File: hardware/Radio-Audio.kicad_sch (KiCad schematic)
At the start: 9 parts, among them J1 Conn_01x02_MountingPin, U1 LM386

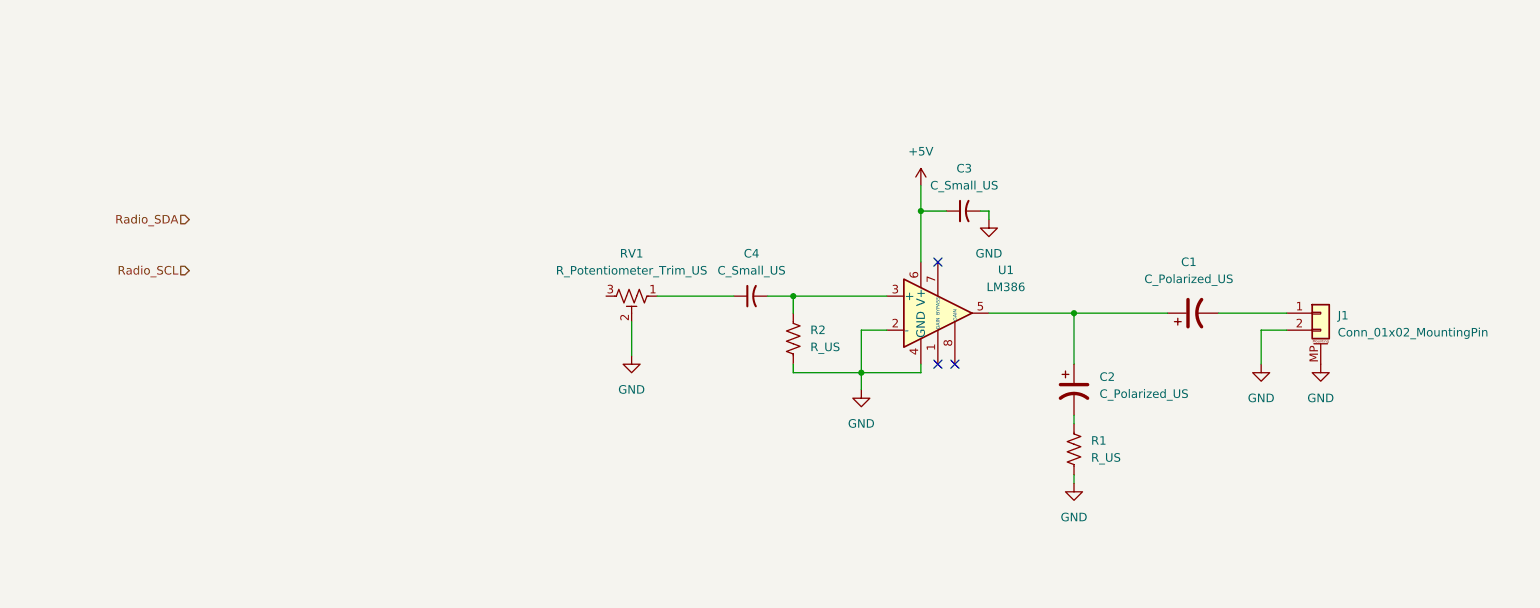
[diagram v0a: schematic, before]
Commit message: Added Radio Module to circuit
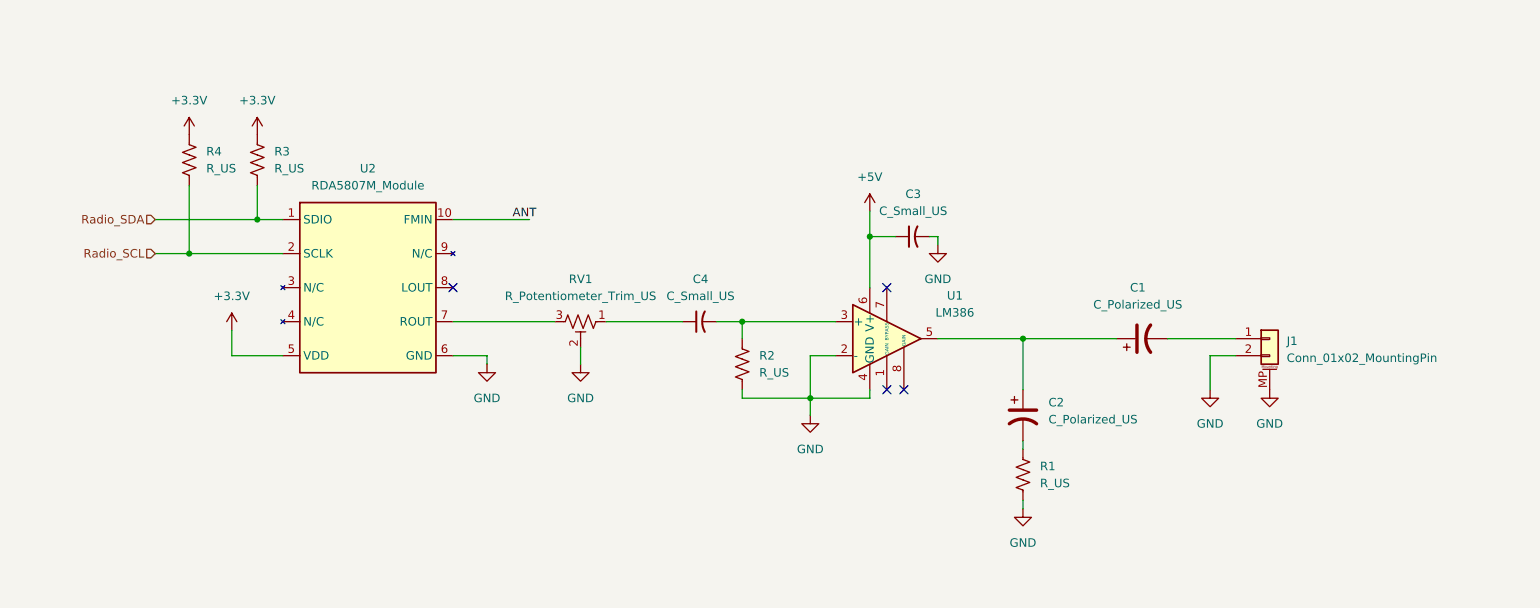
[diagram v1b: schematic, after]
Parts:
- added R3, R4: R_US, symbol Device:R_US
- added U2: RDA5807M_Module, ECE:RDA5807M_Module_TH, symbol ECE:RDA5807M_Module
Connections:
- net GND: now also U2.6 (GND)
- net Radio_SCL: now also R4.2, U2.2 (SCLK)
- net Radio_SDA: now also R3.1, U2.1 (SDIO)
- net at RV1.3: now also U2.7 (ROUT)
- new net +3.3V: R3.2, R4.1, U2.5 (VDD)
- new net ANT: U2.10 (FMIN)
- no-connect marks 3 -> 4
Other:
- moved on the sheet: C1, C2, C3, C4, J1, R1, R2, RV1, U1

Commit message: Assigned Pinout to Subsystems
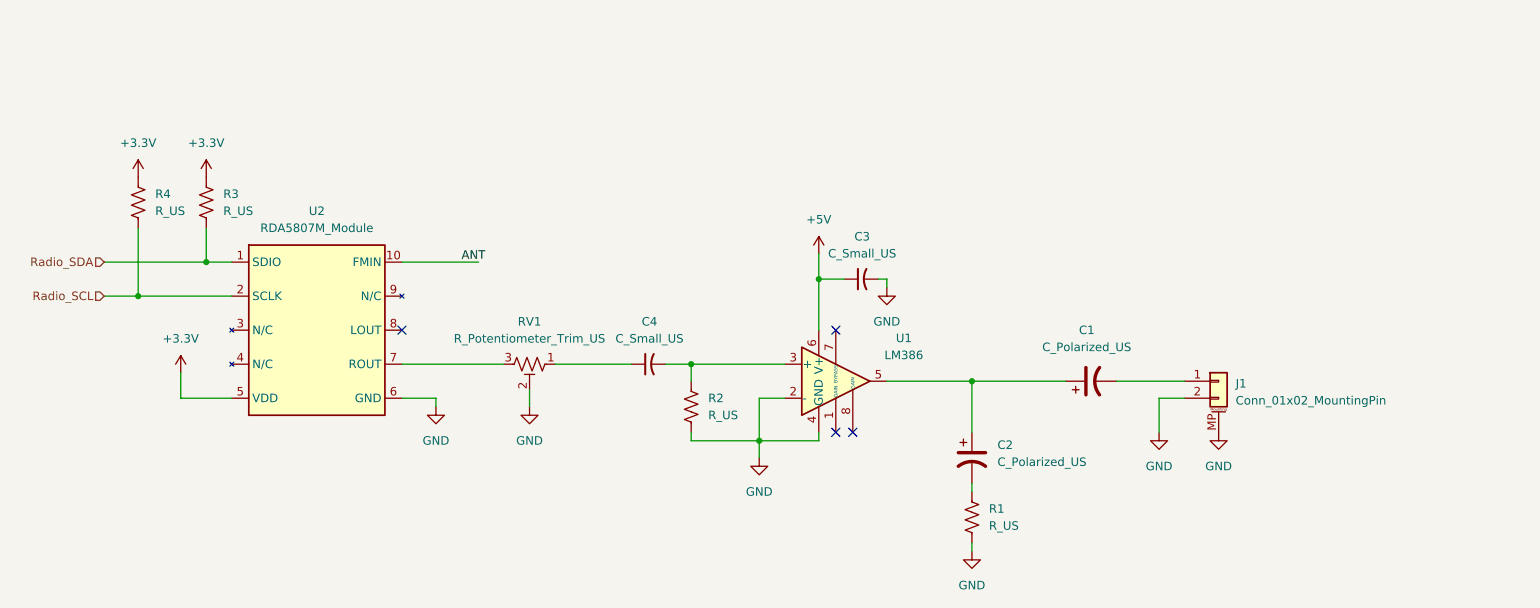
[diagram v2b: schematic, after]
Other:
- moved on the sheet: C1, C2, C3, C4, J1, R1, R2, R3, R4, RV1, U1, U2

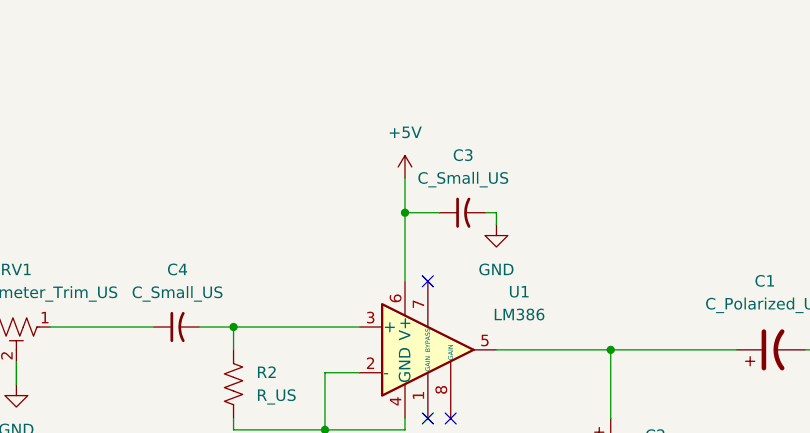
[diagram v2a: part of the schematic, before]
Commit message: Powerchain
Powerchain first draft done
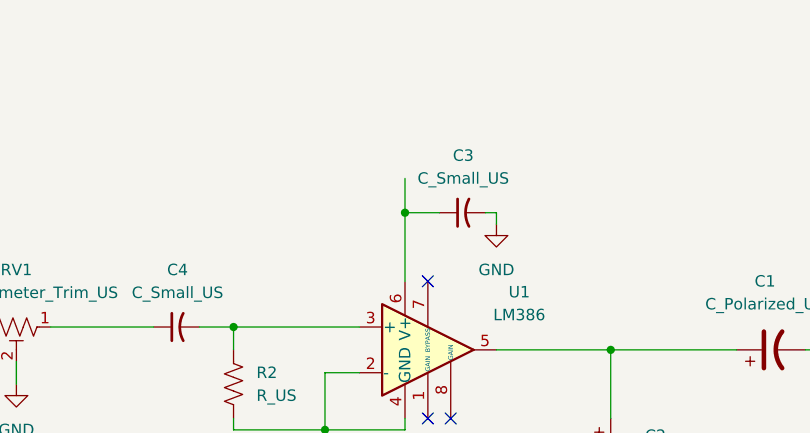
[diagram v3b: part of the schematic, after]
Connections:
- net +5V: no longer names the net of C3.1, U1.6 (V+)
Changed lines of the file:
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@@
-	)
-	(symbol
-		(lib_id "power:+5V")
-		(at 167.64 86.36 0)
-		(unit 1)
-		(exclude_from_sim no)
-		(in_bom yes)
-		(on_board yes)
-		(dnp no)
-		(fields_autoplaced yes)
-		(property "Reference" "#PWR07"
-			(at 167.64 90.17 0)
-			(effects
-				(font
-					(size 1.27 1.27)
-				)
-				(hide yes)
-			)
-		)
-		(property "Value" "+5V"
-			(at 167.64 81.28 0)
-			(effects
-				(font
-					(size 1.27 1.27)
-				)
-			)
-		)
-		(property "Footprint" ""
-			(at 167.64 86.36 0)
-			(effects
-				(font
-					(size 1.27 1.27)
-				)
-				(hide yes)
-			)
-		)
-		(property "Datasheet" ""
-			(at 167.64 86.36 0)
-			(effects
-				(font
-					(size 1.27 1.27)
-				)
-				(hide yes)
-			)
-		)
-		(property "Description" "Power symbol creates a global label with name \"+5V\""
-			(at 167.64 86.36 0)
-			(effects
-				(font
-					(size 1.27 1.27)
-				)
-				(hide yes)
-			)
-		)
-		(pin "1"
-		)
-		(instances
-			(project ""
-				(path "/adf646d2-aa7c-4345-9423-7107505b3b06/1b91a94e-3823-4ebf-b09f-64912f681b22"
-					(reference "#PWR07")
-					(unit 1)
-				)
-			)
-		)
 	)
 	(symbol

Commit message: Added Button circuit
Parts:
- added AE1: Antenna, symbol Device:Antenna
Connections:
- net +5V: now reaches C3.1, U1.6 (V+)
- net ANT: no longer names the net of U2.10 (FMIN)
- net ANT: now also AE1.1 (A)
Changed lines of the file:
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@@
-	(wire
-		(pts
-			(xy 105.41 87.63) (xy 116.84 87.63)
-		)
-		(stroke
-			(width 0)
-			(type default)
-		)
-	)
 	(wire
 		(pts
@@
 	(wire
 		(pts
+			(xy 105.41 87.63) (xy 113.03 87.63)
+		)
+		(stroke
+			(width 0)
+			(type default)
+		)
+	)
+	(wire
+		(pts
 			(xy 190.5 105.41) (xy 190.5 113.03)
 		)
@@
 	(wire
 		(pts
+			(xy 113.03 87.63) (xy 113.03 80.01)
+		)
+		(stroke
+			(width 0)
+			(type default)
+		)
+	)
+	(wire
+		(pts
 			(xy 148.59 114.3) (xy 158.75 114.3)
 		)
@@
 			(width 0)
 			(type default)
-		)
-	)
-	(label "ANT"
-		(at 114.3 87.63 0)
-		(effects
-			(font
-				(size 1.27 1.27)
-			)
-			(justify left bottom)
 		)
 	)
@@
 	)
 	(symbol
+		(lib_id "Device:Antenna")
+		(at 113.03 74.93 0)
+		(unit 1)
+		(exclude_from_sim no)
+		(in_bom yes)
+		(on_board yes)
+		(dnp no)
+		(fields_autoplaced yes)
+		(property "Reference" "AE1"
+			(at 115.57 74.2949 0)
+			(effects
+				(font
+					(size 1.27 1.27)
+				)
+				(justify left)
+			)
+		)
+		(property "Value" "Antenna"
+			(at 115.57 76.8349 0)
+			(effects
+				(font
+					(size 1.27 1.27)
+				)
+				(justify left)
+			)
+		)
+		(property "Footprint" ""
+			(at 113.03 74.93 0)
+			(effects
+				(font
+					(size 1.27 1.27)
+				)
+				(hide yes)
+			)
+		)
+		(property "Datasheet" "~"
+			(at 113.03 74.93 0)
+			(effects
+				(font
+					(size 1.27 1.27)
+				)
+				(hide yes)
+			)
+		)
+		(property "Description" "Antenna"
+			(at 113.03 74.93 0)
+			(effects
+				(font
+					(size 1.27 1.27)
+				)
+				(hide yes)
+			)
+		)
+		(pin "1"
+		)
+		(instances
+			(project ""
+				(path "/adf646d2-aa7c-4345-9423-7107505b3b06/1b91a94e-3823-4ebf-b09f-64912f681b22"
+					(reference "AE1")
+					(unit 1)
+				)
+			)
+		)
+	)
+	(symbol
 		(lib_id "Device:R_US")
 		(at 148.59 109.22 0)
@@
 					(unit 1)
 				)
+			)
+		)
+	)
+	(symbol
+		(lib_id "power:+5V")
+		(at 167.64 86.36 0)
+		(unit 1)
+		(exclude_from_sim no)
+		(in_bom yes)
+		(on_board yes)
+		(dnp no)
+		(fields_autoplaced yes)
+		(property "Reference" "#PWR028"
+			(at 167.64 90.17 0)
+			(effects
+				(font
+					(size 1.27 1.27)
+				)
+				(hide yes)
+			)
+		)
+		(property "Value" "+5V"
+			(at 167.64 81.28 0)
+			(effects
+				(font
+					(size 1.27 1.27)
+				)
+			)
+		)
+		(property "Footprint" ""
+			(at 167.64 86.36 0)
+			(effects
+				(font
+					(size 1.27 1.27)
+				)
+				(hide yes)
+			)
+		)
+		(property "Datasheet" ""
+			(at 167.64 86.36 0)
+			(effects
+				(font
+					(size 1.27 1.27)
+				)
+				(hide yes)
+			)
+		)
+		(property "Description" "Power symbol creates a global label with name \"+5V\""
+			(at 167.64 86.36 0)
+			(effects
+				(font
+					(size 1.27 1.27)
+				)
+				(hide yes)
+			)
+		)
+		(pin "1"
+		)
+		(instances
+			(project ""
+				(path "/adf646d2-aa7c-4345-9423-7107505b3b06/1b91a94e-3823-4ebf-b09f-64912f681b22"
+					(reference "#PWR028")
+					(unit 1)
+				)

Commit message: Rough Board Layout
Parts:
- removed C2: C_Polarized_US, symbol Device:C_Polarized_US
- removed J1: Conn_01x02_MountingPin, symbol Connector_Generic_MountingPin:Conn_01x02_MountingPin
- added C2: 0.047uF, Capacitor_SMD:C_1812_4532Metric, symbol Device:C_US
- added LS1: Speaker, Connector_PinHeader_2.00mm:PinHeader_1x02_P2.00mm_Vertical, symbol Device:Speaker
- AE1: footprint (none) -> Package_TO_SOT_SMD:SOT-23-3
- C1: value C_Polarized_US -> 470uF; footprint (none) -> Capacitor_SMD:CP_Elec_8x10
- C3, C4: value C_Small_US -> 10uF; footprint (none) -> Capacitor_SMD:C_1812_4532Metric
- R1: value R_US -> 10Ω; footprint (none) -> Resistor_SMD:R_1812_4532Metric
- R2: value R_US -> 10kΩ; footprint (none) -> Resistor_SMD:R_1812_4532Metric
- R3, R4: value R_US -> 2kΩ; footprint (none) -> Resistor_SMD:R_1812_4532Metric
- RV1: footprint (none) -> Potentiometer_SMD:Potentiometer_Bourns_3314J_Vertical
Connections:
- net GND: now also LS1.2
- net at R1.1: now also C2.2
- net at C1.1, U1.5: now also C2.1
- net at C1.2: now also LS1.1
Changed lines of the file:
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@@
 			)
 		)
-		(property "Value" "C_Small_US"
+		(property "Value" "10uF"
 			(at 174.117 86.36 90)
 			(effects
@@
 			)
 		)
-		(property "Footprint" ""
+		(property "Footprint" "Capacitor_SMD:C_1812_4532Metric"
 			(at 173.99 90.17 0)
 			(effects
@@
 			)
 		)
-		(property "Value" "R_US"
+		(property "Value" "10Ω"
 			(at 193.04 126.9999 0)
 			(effects
@@
 			)
 		)
-		(property "Footprint" ""
+		(property "Footprint" "Resistor_SMD:R_1812_4532Metric"
 			(at 191.516 125.984 90)
 			(effects
@@
 			)
 		)
-		(property "Footprint" ""
+		(property "Footprint" "Potentiometer_SMD:Potentiometer_Bourns_3314J_Vertical"
 			(at 124.46 102.87 0)
 			(effects
@@
 	)
 	(symbol
+		(lib_id "Device:C_US")
+		(at 190.5 116.84 0)
+		(unit 1)
+		(exclude_from_sim no)
+		(in_bom yes)
+		(on_board yes)
+		(dnp no)
+		(fields_autoplaced yes)
+		(property "Reference" "C2"
+			(at 194.31 115.8239 0)
+			(effects
+				(font
+					(size 1.27 1.27)
+				)
+				(justify left)
+			)
+		)
+		(property "Value" "0.047uF"
+			(at 194.31 118.3639 0)
+			(effects
+				(font
+					(size 1.27 1.27)
+				)
+				(justify left)
+			)
+		)
+		(property "Footprint" "Capacitor_SMD:C_1812_4532Metric"
+			(at 190.5 116.84 0)
+			(effects
+				(font
+					(size 1.27 1.27)
+				)
+				(hide yes)
+			)
+		)
+		(property "Datasheet" ""
+			(at 190.5 116.84 0)
+			(effects
+				(font
+					(size 1.27 1.27)
+				)
+				(hide yes)
+			)
+		)
+		(property "Description" "capacitor, US symbol"
+			(at 190.5 116.84 0)
+			(effects
+				(font
+					(size 1.27 1.27)
+				)
+				(hide yes)
+			)
+		)
+		(pin "1"
+		)
+		(pin "2"
+		)
+		(instances
+			(project ""
+				(path "/adf646d2-aa7c-4345-9423-7107505b3b06/1b91a94e-3823-4ebf-b09f-64912f681b22"
+					(reference "C2")
+					(unit 1)
+				)
+			)
+		)
+	)
+	(symbol
 		(lib_id "power:+3.3V")
 		(at 66.04 74.93 0)
@@
 	)
 	(symbol
-		(lib_id "Device:C_Polarized_US")
-		(at 190.5 116.84 0)
-		(unit 1)
-		(exclude_from_sim no)
-		(in_bom yes)
-		(on_board yes)
-		(dnp no)
-		(fields_autoplaced yes)
-		(property "Reference" "C2"
-			(at 194.31 114.9349 0)
-			(effects
-				(font
-					(size 1.27 1.27)
-				)
-				(justify left)
-			)
-		)
-		(property "Value" "C_Polarized_US"
-			(at 194.31 117.4749 0)
-			(effects
-				(font
-					(size 1.27 1.27)
-				)
-				(justify left)
-			)
-		)
-		(property "Footprint" ""
-			(at 190.5 116.84 0)
-			(effects
-				(font
-					(size 1.27 1.27)
-				)
-				(hide yes)
-			)
-		)
-		(property "Datasheet" "~"
-			(at 190.5 116.84 0)
-			(effects
-				(font
-					(size 1.27 1.27)
-				)
-				(hide yes)
-			)
-		)
-		(property "Description" "Polarized capacitor, US symbol"
-			(at 190.5 116.84 0)
-			(effects
-				(font
-					(size 1.27 1.27)
-				)
-				(hide yes)
-			)
-		)
-		(pin "2"
-		)
-		(pin "1"
-		)
-		(instances
-			(project ""
-				(path "/adf646d2-aa7c-4345-9423-7107505b3b06/1b91a94e-3823-4ebf-b09f-64912f681b22"
-					(reference "C2")
-					(unit 1)
-				)
-			)
-		)
-	)
-	(symbol
-		(lib_id "power:GND")
-		(at 227.33 113.03 0)
-		(unit 1)
-		(exclude_from_sim no)
-		(in_bom yes)
-		(on_board yes)
-		(dnp no)
-		(fields_autoplaced yes)
-		(property "Reference" "#PWR05"
-			(at 227.33 119.38 0)
-			(effects
-				(font
-					(size 1.27 1.27)
-				)
-				(hide yes)
-			)
-		)
-		(property "Value" "GND"
-			(at 227.33 118.11 0)
-			(effects
-				(font
-					(size 1.27 1.27)
-				)
-			)
-		)
-		(property "Footprint" ""
-			(at 227.33 113.03 0)
-			(effects
-				(font
-					(size 1.27 1.27)
-				)
-				(hide yes)
-			)
-		)
-		(property "Datasheet" ""
-			(at 227.33 113.03 0)
-			(effects
-				(font
-					(size 1.27 1.27)
-				)
-				(hide yes)
-			)
-		)
-		(property "Description" "Power symbol creates a global label with name \"GND\" , ground"
-			(at 227.33 113.03 0)
-			(effects
-				(font
-					(size 1.27 1.27)
-				)
-				(hide yes)
-			)
-		)
-		(pin "1"
-		)
-		(instances
-			(project "Main"
-				(path "/adf646d2-aa7c-4345-9423-7107505b3b06/1b91a94e-3823-4ebf-b09f-64912f681b22"
-					(reference "#PWR05")
-					(unit 1)
-				)
-			)
-		)
-	)
-	(symbol
 		(lib_id "power:GND")
 		(at 218.44 113.03 0)
@@
 			)
 		)
-		(property "Footprint" ""
+		(property "Footprint" "Package_TO_SOT_SMD:SOT-23-3"
 			(at 113.03 74.93 0)
 			(effects
@@
 			)
 		)
-		(property "Value" "R_US"
+		(property "Value" "10kΩ"
 			(at 151.13 110.4899 0)
 			(effects
@@
 			)
 		)
-		(property "Footprint" ""
+		(property "Footprint" "Resistor_SMD:R_1812_4532Metric"
 			(at 149.606 109.474 90)
 			(effects
@@
 	)
 	(symbol
-		(lib_id "Connector_Generic_MountingPin:Conn_01x02_MountingPin")
-		(at 227.33 105.41 0)
-		(unit 1)
-		(exclude_from_sim no)
-		(in_bom yes)
-		(on_board yes)
-		(dnp no)
-		(fields_autoplaced yes)
-		(property "Reference" "J1"
-			(at 229.87 105.7655 0)
-			(effects
-				(font
-					(size 1.27 1.27)
-				)
-				(justify left)
-			)
-		)
-		(property "Value" "Conn_01x02_MountingPin"
-			(at 229.87 108.3055 0)
-			(effects
-				(font
-					(size 1.27 1.27)
-				)
-				(justify left)
-			)
-		)
-		(property "Footprint" ""
-			(at 227.33 105.41 0)
-			(effects
-				(font
-					(size 1.27 1.27)
-				)
-				(hide yes)
-			)
-		)
-		(property "Datasheet" "~"
-			(at 227.33 105.41 0)
-			(effects
-				(font
-					(size 1.27 1.27)
-				)
-				(hide yes)
-			)
-		)
-		(property "Description" "Generic connectable mounting pin connector, single row, 01x02, script generated (kicad-library-utils/schlib/autogen/connector/)"
-			(at 227.33 105.41 0)
-			(effects
-				(font
-					(size 1.27 1.27)
-				)
-				(hide yes)
-			)
-		)
-		(pin "MP"
-		)
-		(pin "2"
-		)
-		(pin "1"
-		)
-		(instances
-			(project ""
-				(path "/adf646d2-aa7c-4345-9423-7107505b3b06/1b91a94e-3823-4ebf-b09f-64912f681b22"
-					(reference "J1")
-					(unit 1)
-				)
-			)
-		)
-	)
-	(symbol
 		(lib_id "Device:C_Polarized_US")
 		(at 208.28 105.41 90)
@@
 			)
 		)
-		(property "Value" "C_Polarized_US"
+		(property "Value" "470uF"
 			(at 207.645 100.33 90)
 			(effects
@@
 			)
 		)
-		(property "Footprint" ""
+		(property "Footprint" "Capacitor_SMD:CP_Elec_8x10"
 			(at 208.28 105.41 0)
 			(effects
@@
 			)
 		)
-		(property "Value" "R_US"
+		(property "Value" "2kΩ"
 			(at 78.74 80.0099 0)
 			(effects
@@
 			)
 		)
-		(property "Footprint" ""
+		(property "Footprint" "Resistor_SMD:R_1812_4532Metric"
 			(at 75.184 78.486 90)
 			(effects
@@
 			)
 		)
-		(property "Value" "R_US"
+		(property "Value" "2kΩ"
 			(at 68.58 80.0099 0)
 			(effects
@@
 			)
 		)
-		(property "Footprint" ""
+		(property "Footprint" "Resistor_SMD:R_1812_4532Metric"
 			(at 67.056 78.994 90)
 			(effects
@@
 			)
 		)
-		(property "Value" "C_Small_US"
+		(property "Value" "10uF"
 			(at 142.367 99.06 90)
 			(effects
@@
 			)
 		)
-		(property "Footprint" ""
+		(property "Footprint" "Capacitor_SMD:C_1812_4532Metric"
 			(at 142.24 102.87 0)
 			(effects
@@
 					(unit 1)
 				)
+			)
+		)
+	)
+	(symbol
+		(lib_id "Device:Speaker")
+		(at 227.33 105.41 0)
+		(unit 1)
+		(exclude_from_sim no)
+		(in_bom yes)
+		(on_board yes)
+		(dnp no)
+		(fields_autoplaced yes)
+		(property "Reference" "LS1"
+			(at 232.41 105.4099 0)
+			(effects
+				(font
+					(size 1.27 1.27)
+				)
+				(justify left)
+			)
+		)
+		(property "Value" "Speaker"
+			(at 232.41 107.9499 0)
+			(effects
+				(font
+					(size 1.27 1.27)
+				)
+				(justify left)
+			)
+		)
+		(property "Footprint" "Connector_PinHeader_2.00mm:PinHeader_1x02_P2.00mm_Vertical"
+			(at 227.33 110.49 0)
+			(effects
+				(font
+					(size 1.27 1.27)
+				)
+				(hide yes)
+			)
+		)
+		(property "Datasheet" "~"
+			(at 227.076 106.68 0)
+			(effects
+				(font
+					(size 1.27 1.27)
+				)
+				(hide yes)
+			)
+		)
+		(property "Description" "Speaker"
+			(at 227.33 105.41 0)
+			(effects
+				(font
+					(size 1.27 1.27)
+				)
+				(hide yes)
+			)
+		)
+		(pin "2"
+		)
+		(pin "1"
+		)
+		(instances
+			(project ""
+				(path "/adf646d2-aa7c-4345-9423-7107505b3b06/1b91a94e-3823-4ebf-b09f-64912f681b22"
+					(reference "LS1")
+					(unit 1)
+				)

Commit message: Revised PCB Layout
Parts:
- AE1: footprint Package_TO_SOT_SMD:SOT-23-3 -> Connector_PinHeader_2.00mm:PinHeader_1x01_P2.00mm_Vertical
- C1: footprint Capacitor_SMD:CP_Elec_8x10 -> Capacitor_Tantalum_SMD:CP_EIA-7343-30_AVX-N
- RV1: value R_Potentiometer_Trim_US -> 10kΩ
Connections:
- net GND: now also RV1.1; no longer RV1.2
- net at C4.1: now also RV1.3; no longer RV1.1
- net at U2.7 (ROUT): now also RV1.2; no longer RV1.3
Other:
- moved on the sheet: C1, C2, C3, C4, LS1, R1, R2, RV1, U1
